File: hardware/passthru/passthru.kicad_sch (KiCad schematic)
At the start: 81 parts, among them J1 ARM_SWD, J2 RJ45_LED_Shielded, J3 Screw_Terminal_01x02, Q1 Q_PMOS_DGS, Q2 Q_PMOS_DGS, Q3 Q_NPN_BEC, U1 EFM32GG11B8xx, U2 KSZ8081RND, U3 LM5085, U4 TPS2375-1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

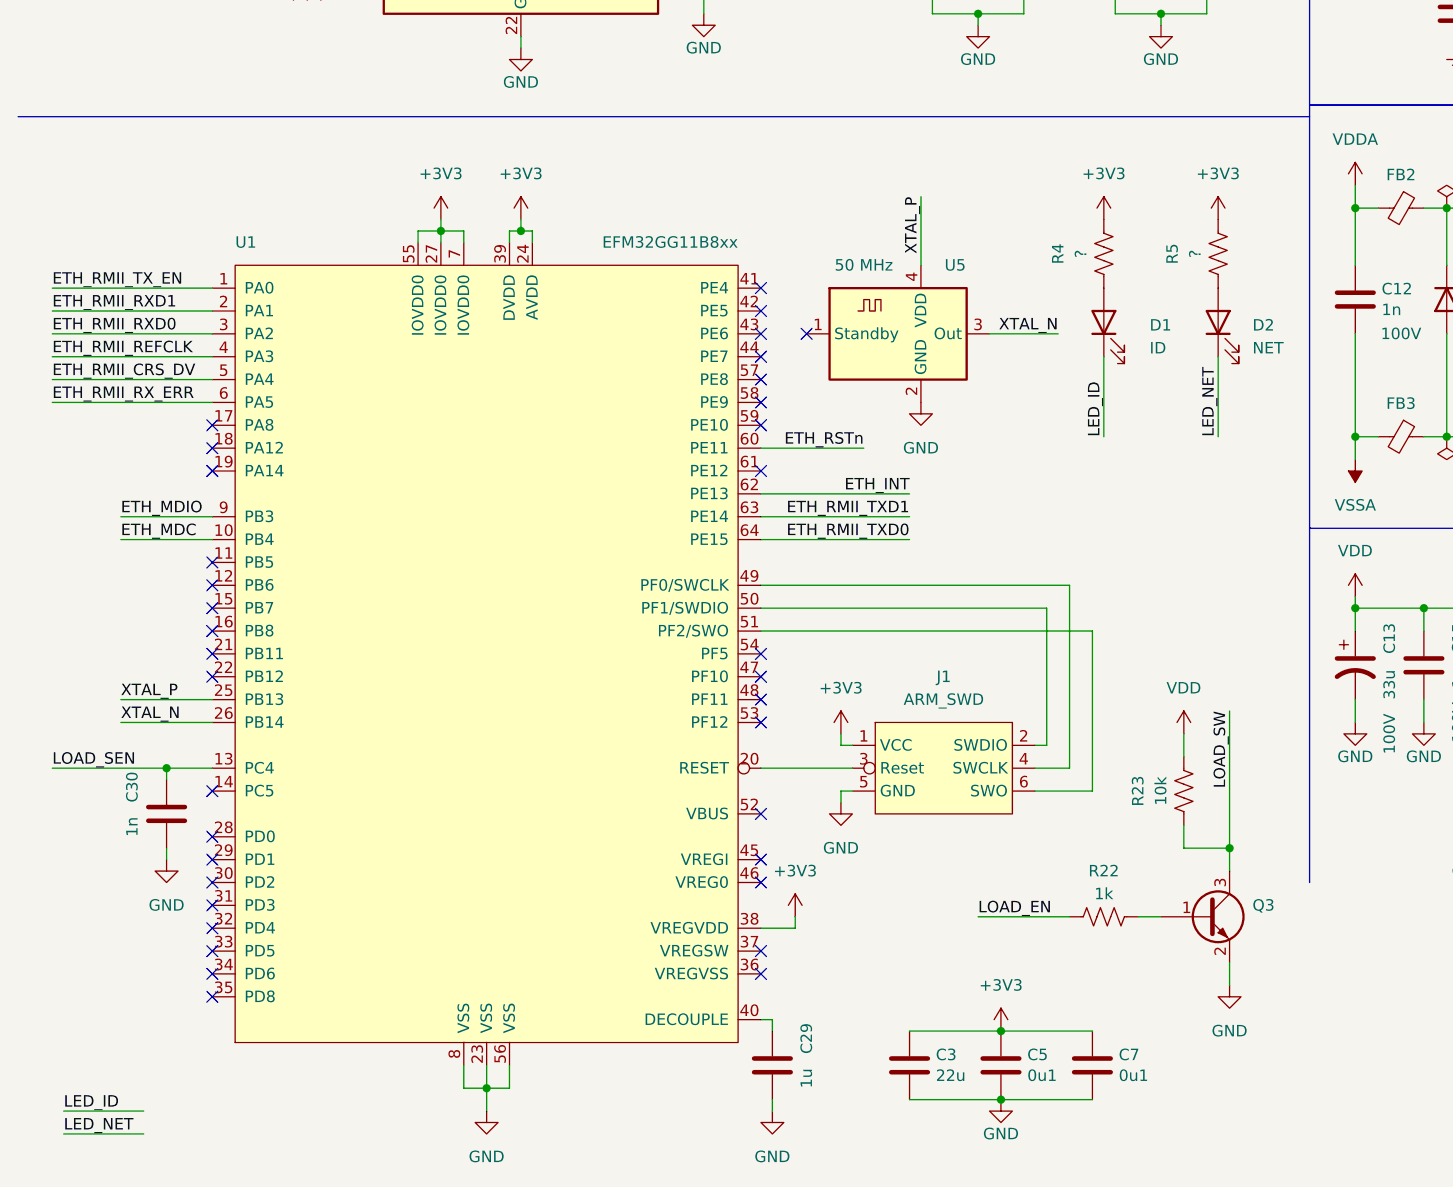
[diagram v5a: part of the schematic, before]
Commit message: passthru: route the signals for the LEDs
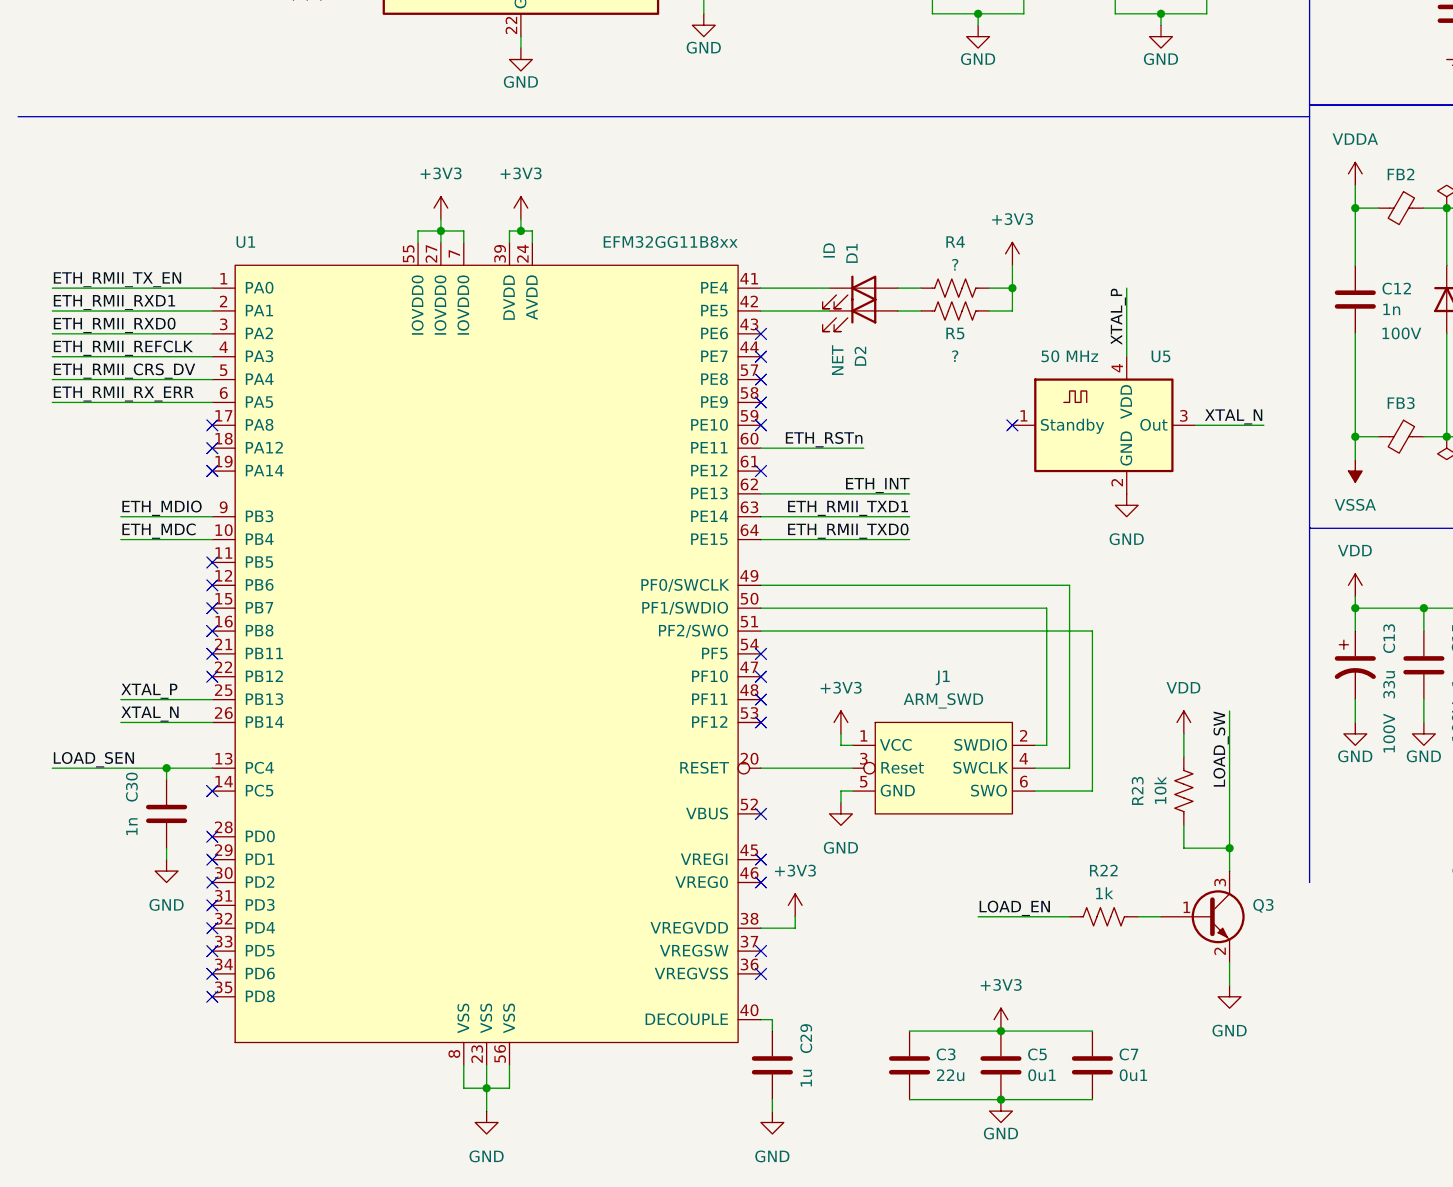
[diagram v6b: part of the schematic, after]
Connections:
- net LED_ID is gone; now on an unnamed net: D1.1 (K)
- net LED_NET is gone; now on an unnamed net: D2.1 (K)
- no-connect marks 38 -> 36
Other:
- moved on the sheet: D1, D2, R4, R5, U5

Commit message: passthru: use local footprint for PFETs
This one has 3D models.
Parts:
- Q1, Q2: footprint Package_SO:PowerPAK_SO-8_Single -> common:PowerPAK_SO-8_Single
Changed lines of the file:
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@@
       (effects (font (size 1.27 1.27)) (justify left) hide)
     )
-    (property "Footprint" "Package_SO:PowerPAK_SO-8_Single" (id 2) (at 234.315 135.89 0)
+    (property "Footprint" "common:PowerPAK_SO-8_Single" (id 2) (at 234.315 135.89 0)
       (effects (font (size 1.27 1.27) italic) (justify left) hide)
     )
@@
       (effects (font (size 1.27 1.27)) hide)
     )
-    (property "Footprint" "Package_SO:PowerPAK_SO-8_Single" (id 2) (at 240.665 99.06 0)
+    (property "Footprint" "common:PowerPAK_SO-8_Single" (id 2) (at 240.665 99.06 0)
       (effects (font (size 1.27 1.27) italic) (justify left) hide)
     )
@@
     )
     (path "/3b171c12-23a9-40c9-8b4b-a2865c498c23"
-      (reference "Q1") (unit 1) (value "Q_PMOS_DGS") (footprint "Package_SO:PowerPAK_SO-8_Single")
+      (reference "Q1") (unit 1) (value "Q_PMOS_DGS") (footprint "common:PowerPAK_SO-8_Single")
     )
     (path "/d50e64c1-165e-4e88-931e-7e1d4303054e"
-      (reference "Q2") (unit 1) (value "Q_PMOS_DGS") (footprint "Package_SO:PowerPAK_SO-8_Single")
+      (reference "Q2") (unit 1) (value "Q_PMOS_DGS") (footprint "common:PowerPAK_SO-8_Single")
     )
     (path "/5ace4dd3-8bbf-416c-b527-4a320e0eb289"

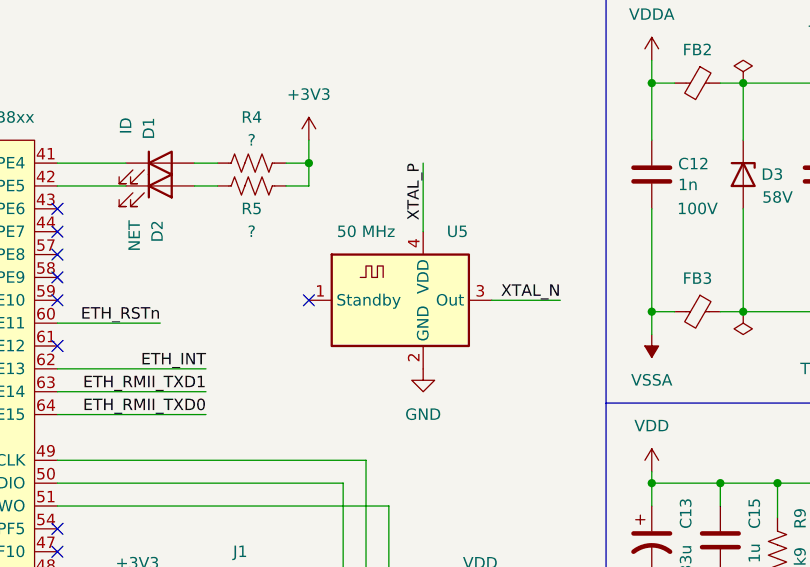
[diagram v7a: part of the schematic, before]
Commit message: passthru: update oscillator
This one has a 3D model.
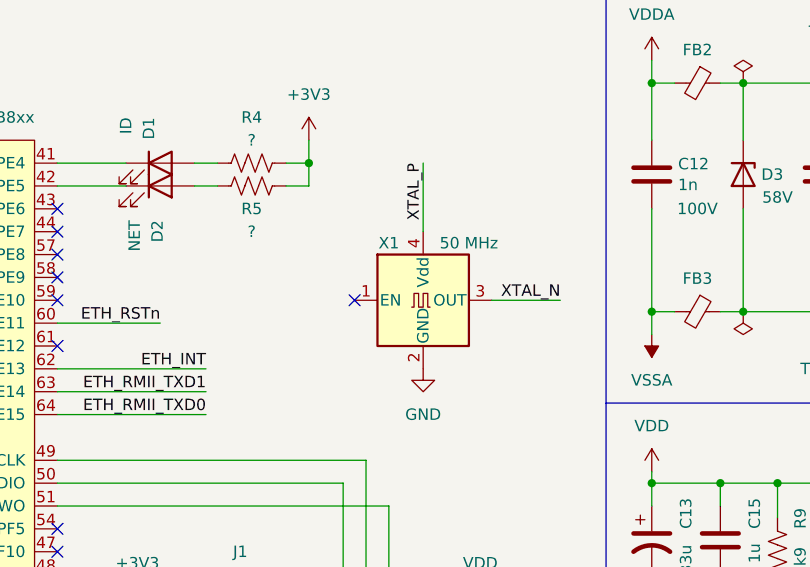
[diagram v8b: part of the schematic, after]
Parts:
- removed U5: 50 MHz, Oscillator:Oscillator_SMD_SeikoEpson_SG210-4Pin_2.5x2.0mm_HandSoldering, symbol Oscillator:ASDMB-xxxMHz
- added X1: 50 MHz, common:Oscillator_SMD_Abracon_ASE-4Pin_3.2x2.5mm, symbol Oscillator:ASE-xxxMHz
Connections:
- net GND: now also X1.2 (GND)
- net XTAL_N: now also X1.3 (OUT)
- net XTAL_P: now also X1.4 (Vdd)
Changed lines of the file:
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@@
   (no_connect (at 96.52 162.56))
   (no_connect (at 35.56 147.32))
-  (no_connect (at 124.46 119.38))
+  (no_connect (at 129.54 119.38))
   (no_connect (at 35.56 134.62))
   (no_connect (at 35.56 121.92))
@@
     (pin "2")
   )
-  (symbol (lib_id "Oscillator:ASDMB-xxxMHz") (at 134.62 119.38 0) (unit 1)
-    (in_bom yes) (on_board yes)
-    (property "Reference" "U5" (id 0) (at 140.97 111.76 0))
-    (property "Value" "50 MHz" (id 1) (at 130.81 111.76 0))
-    (property "Footprint" "Oscillator:Oscillator_SMD_SeikoEpson_SG210-4Pin_2.5x2.0mm_HandSoldering" (id 2) (at 134.62 119.38 0)
-      (effects (font (size 1.27 1.27)) hide)
-    )
-    (property "Datasheet" "https://abracon.com/Oscillators/ASDMB.pdf" (id 3) (at 142.24 107.95 0)
-      (effects (font (size 1.27 1.27)) hide)
-    )
-    (pin "1")
-    (pin "2")
-    (pin "3")
-    (pin "4")
-  )
   (symbol (lib_id "power:VSS") (at 212.09 120.65 180) (unit 1)
     (in_bom yes) (on_board yes) (fields_autoplaced)
@@
     (pin "2")
   )
+  (symbol (lib_id "Oscillator:ASE-xxxMHz") (at 137.16 119.38 0) (unit 1)
+    (in_bom yes) (on_board yes)
+    (property "Reference" "X1" (id 0) (at 133.35 113.03 0))
+    (property "Value" "50 MHz" (id 1) (at 142.24 113.03 0))
+    (property "Footprint" "common:Oscillator_SMD_Abracon_ASE-4Pin_3.2x2.5mm" (id 2) (at 154.94 128.27 0)
+      (effects (font (size 1.27 1.27)) hide)
+    )
+    (property "Datasheet" "http://www.abracon.com/Oscillators/ASV.pdf" (id 3) (at 134.62 119.38 0)
+      (effects (font (size 1.27 1.27)) hide)
+    )
+    (pin "1")
+    (pin "2")
+    (pin "3")
+    (pin "4")
+  )
   (symbol (lib_id "Device:R_US") (at 199.39 100.33 0) (mirror x) (unit 1)
     (in_bom yes) (on_board yes)
@@
       (reference "U4") (unit 1) (value "TPS2375-1") (footprint "Package_SO:TSSOP-8_4.4x3mm_P0.65mm")
     )
-    (path "/3f9cf990-be2c-4ae1-aa3d-8f13db44adf7"
-      (reference "U5") (unit 1) (value "50 MHz") (footprint "Oscillator:Oscillator_SMD_SeikoEpson_SG210-4Pin_2.5x2.0mm_HandSoldering")
+    (path "/a926071f-44d9-4895-b803-f5b2dba1bd4a"
+      (reference "X1") (unit 1) (value "50 MHz") (footprint "common:Oscillator_SMD_Abracon_ASE-4Pin_3.2x2.5mm")
     )
   )
